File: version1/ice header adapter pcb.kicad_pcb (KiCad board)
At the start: 2 copper layers, 48.3 x 48.3 mm, 13 parts, among them P1 TST, P2 TST, P3 TST, P4 TST

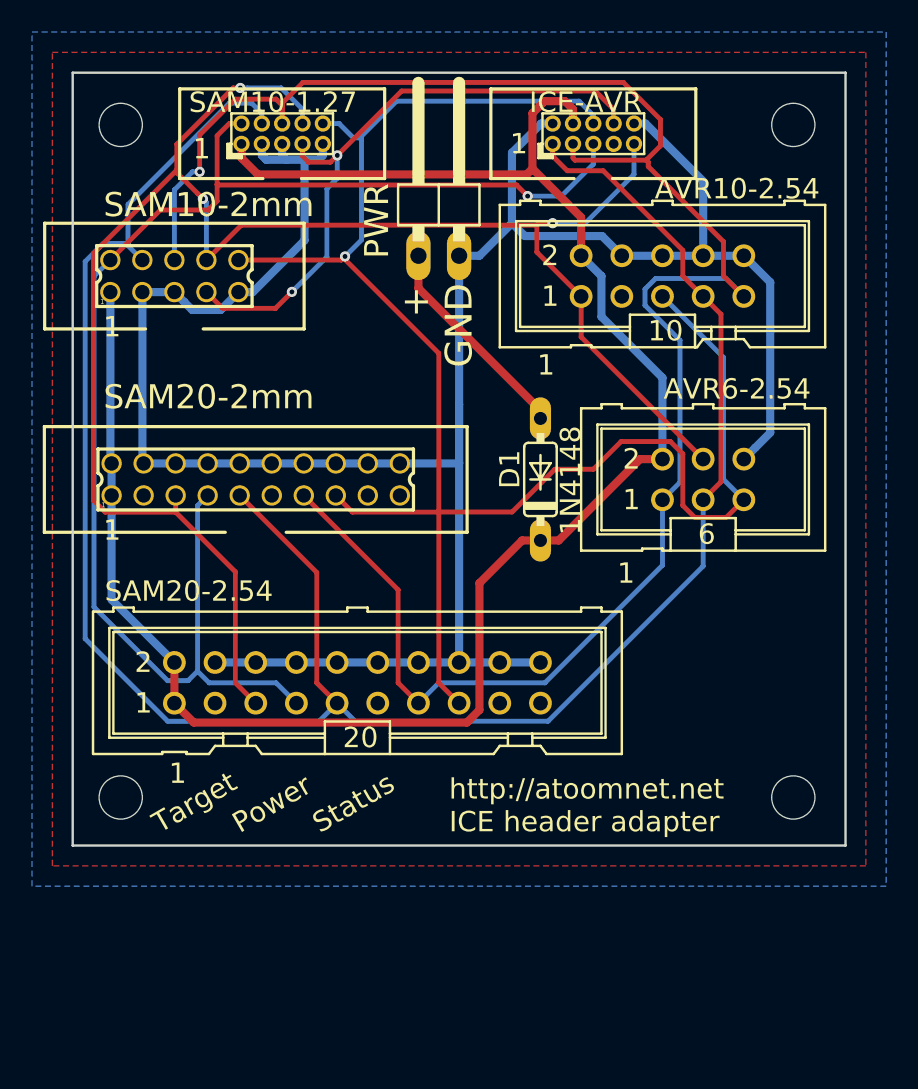
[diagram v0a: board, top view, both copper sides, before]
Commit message: UPDI -ISP
SAM delete
UPDI 10p. added
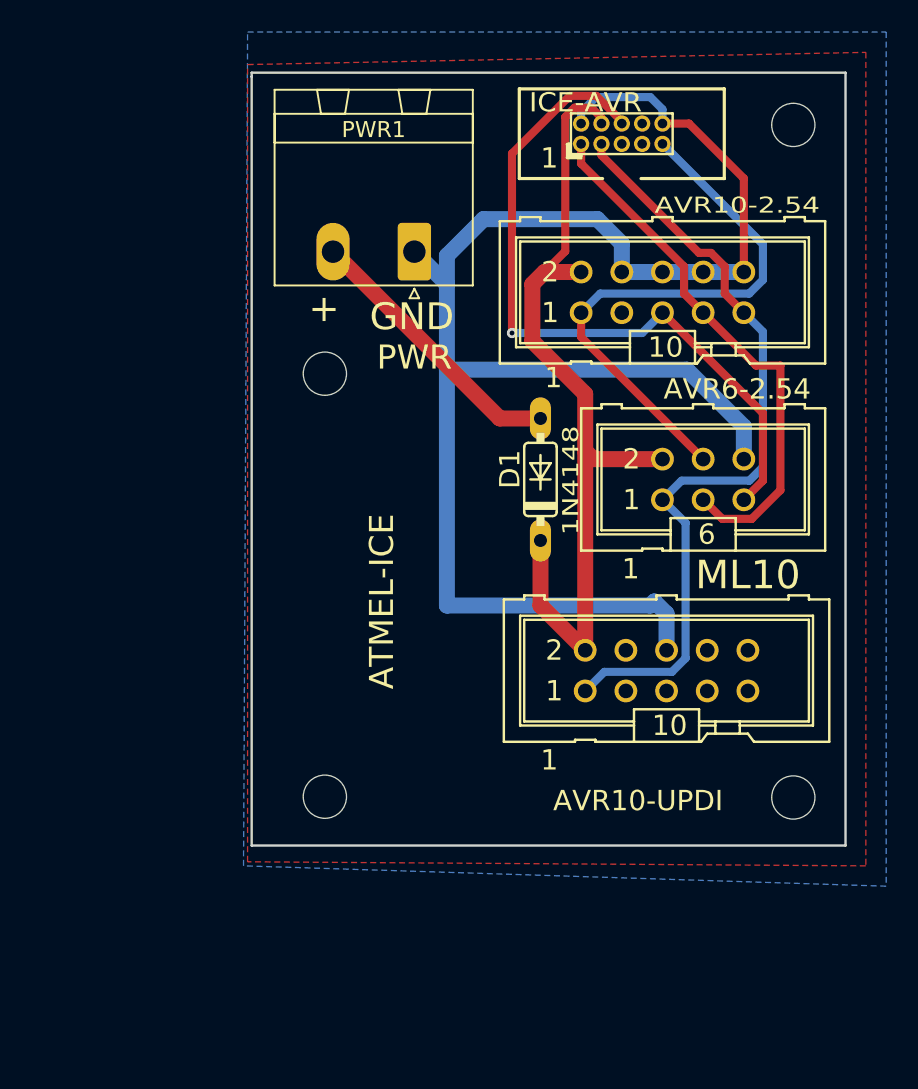
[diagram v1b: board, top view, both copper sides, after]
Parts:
- removed SAM10-1.27: PINHEAD_PINHD-2X5, Arduino_Wifi_shield_v018_tG:PINHEAD_2X05_127
- removed SAM10-2: 87758-1016, con-molex:87758-1016
- removed SAM20-2: 87758-2016, con-molex:87758-2016
- removed SAM20-2.54: ML20, con-harting-ml:ML20
- added AVR10-UPDI: ML10, con-harting-ml:ML10, F.Cu at (87.9, 149.1)
- PWR1: value PINHD-1X2 -> Screw_Terminal_01x02; footprint pinhead:1X02_90 -> Connector_Phoenix_MSTB:PhoenixContact_MSTBA_2,5_2-G-5,08_1x02_P5.08mm_Horizontal
- moved P1 20.1 mm to (66.5, 130.6)
- moved P3 12.7 mm to (66.5, 157.0)
- moved PWR1 3.87 mm to (72.1, 122.9), turned to 180 degrees
- moved ICE-AVR1 1.78 mm to (85.1, 115.6)
- moved AVR10-2.54 1.02 mm to (87.6, 125.5)
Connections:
- AVR10-2.54 pad 3: (no net) -> unconnected-(AVR10-2.54-Pad3)
- ICE-AVR1 pad 7: (no net) -> unconnected-(ICE-AVR1-Pad7)
- PWR1 pad 1: Net-(D1-PadA) -> /GND
- PWR1 pad 2: /GND -> Net-(D1-PadA)
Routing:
- net /TCK: track 136.1 -> 33.7 mm
- net /TMS: track 88.9 -> 0.00 mm, vias 1 -> 0
- net /TDI: track 111.7 -> 35.6 mm, vias 3 -> 0
- net /TDO: track 122.2 -> 49.5 mm, vias 1 -> 0
- net /NSRST: track 111.4 -> 45.0 mm
- net /VTG: track 118.3 -> 55.1 mm
- net /GND: track 155.5 -> 104.8 mm
- net /NTRST: track 39.4 -> 0.00 mm, vias 2 -> 0
- net Net-(D1-PadA): track 13.3 -> 17.3 mm
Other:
- board size 48.3 x 48.3 mm -> 37.1 x 48.3 mm
- net class Default removed
- net class power removed
- board text added: "ATMEL-ICE"
- board text removed: "Power"
- board text removed: "SAM10-1.27"
- board text removed: "SAM10-2mm"
- board text removed: "SAM20-2mm"
- board text removed: "Status"
- board text removed: "Target"
- board text removed: "http://atoomnet.net ICE header adapter"

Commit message: weiter am pc
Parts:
- added Avr1: JTAG, con-harting-ml:ML10, F.Cu at (87.6, 161.3)
- added J1: FTDI 232, Connector_PinSocket_2.54mm:PinSocket_1x06_P2.54mm_Vertical, F.Cu at (60.4, 151.2)
- added JP1: FTDI_VCC, Connector_PinSocket_2.54mm:PinSocket_1x02_P2.54mm_Vertical, F.Cu at (60.3, 141.6)
- added SW1: Reset, Button_Switch_THT:SW_PUSH_6mm_H5mm, F.Cu at (59.6, 129.8)
- moved P1 17.1 mm to (59.7, 114.9)
- moved P3 14.3 mm to (59.7, 169.5)
- moved P4 12.5 mm to (95.9, 169.5)
- renumbered AVR10-2.54 to AVR10-2.1, AVR6-2.54 to AVR6-2.1, AVR10-UPDI to UPDI
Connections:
- UPDI pad 3: unconnected-(AVR10-UPDI1-Pad3) -> /RX
- UPDI pad 4: unconnected-(AVR10-UPDI1-Pad4) -> /TX
- UPDI pad 5: unconnected-(AVR10-UPDI1-Pad5) -> /RESET
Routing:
- net /GND: track 104.8 -> 0.00 mm
- net /VTG: track 55.1 -> 0.00 mm
- net /TDO: track 49.5 -> 0.00 mm
- net /NSRST: track 45.0 -> 0.00 mm, vias 1 -> 0
- net /TDI: track 35.6 -> 0.00 mm
- net /TCK: track 33.7 -> 0.00 mm
- net Net-(D1-PadA): track 17.3 -> 0.00 mm
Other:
- board size 37.1 x 48.3 mm -> 43.2 x 61 mm
- board text added: "ISP"
- board text added: "SPI"
- board text added: "aWire"
